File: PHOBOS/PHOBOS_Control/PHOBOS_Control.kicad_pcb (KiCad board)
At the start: 2 copper layers, 125.4 x 71.6 mm, 76 parts, among them J1 Screw_Terminal_01x02, J2 Conn_01x06, J3 Conn_Coaxial, J5 DE9_Pins_MountingHoles, J6 USB4056-03-A_REVA2, U1 SX1280IMLTRT, U2 TLV9351IDCKR, U3 W25Q128JVSIQ, U4 NCP1117-3.3_SOT223, U5 RP2040, U6 TLV9351IDCKR, U7 TLV9351IDCKR, U8 TLV9351IDCKR, Y1 ABM8-272-T3, Y2 C1E-52.000-10-1012-X-M

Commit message: some routing added. op amps rearranged
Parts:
- moved C14 47.2 mm to (138.2, 367.5)
- moved D1 47.2 mm to (143.1, 364.1)
- moved C12 47.2 mm to (139.9, 367.5)
- moved C13 47.2 mm to (141.5, 367.5)
- moved D4 47.2 mm to (143.1, 367.5)
- moved J1 47.2 mm to (146.5, 361.5)
- moved R9 47.2 mm to (133.9, 362.3)
- moved U4 47.2 mm to (138.3, 360.9)
- moved D5 47.2 mm to (132.5, 361.5)
- moved Y2 26.6 mm to (145.2, 397.0)
- moved L1 19.1 mm to (154.2, 391.8)
- moved L2 15.1 mm to (150.4, 390.5)
- moved R15 15.1 mm to (150.4, 392.5)
- moved C37 13.4 mm to (161.9, 364.3)
- moved R12 13.4 mm to (157.4, 364.3)
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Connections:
- C30 pad 1: /PS1MCU -> /PS4MCU
- C31 pad 1: /PS1 -> /PS4
- C32 pad 1: /PS2MCU -> /PS3MCU
- C33 pad 1: /PS2 -> /PS3
- C34 pad 1: /PS3MCU -> /PS2MCU
- C35 pad 1: /PS3 -> /PS2
- C36 pad 1: /PS4MCU -> /PS1MCU
- C37 pad 1: /PS4 -> /PS1
- J5 pad 1: unconnected-(J5-Pad1) -> /PS4
- J5 pad 2: /PS4 -> /PS3
- J5 pad 3: /PS3 -> /PS2
- J5 pad 4: /PS2 -> /PS1
- J5 pad 5: /PS1 -> unconnected-(J5-Pad5)
- R13 pad 2: /PS4 -> /PS1
- R2 pad 2: /PS1 -> /PS4
- R4 pad 2: /PS2 -> /PS3
- R8 pad 2: /PS3 -> /PS2
- U2 pad 1: /PS1MCU -> /PS4MCU
- U2 pad 4: /PS1 -> /PS4
- U5 pad 28: /PS1MCU -> /PS4MCU
- U5 pad 29: /PS2MCU -> /PS3MCU
- U5 pad 30: /PS3MCU -> /PS2MCU
- U5 pad 31: /PS4MCU -> /PS1MCU
- U6 pad 1: /PS2MCU -> /PS3MCU
- U6 pad 4: /PS2 -> /PS3
- U7 pad 1: /PS3MCU -> /PS2MCU
- U7 pad 4: /PS3 -> /PS2
- U8 pad 1: /PS4MCU -> /PS1MCU
- U8 pad 4: /PS4 -> /PS1
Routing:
- net +BATT: track 4.14 -> 39.5 mm, vias 0 -> 4
- net +3V3: track 0.00 -> 22.7 mm
- net /PS1: track 0.00 -> 9.35 mm
- net /PS4: track 0.00 -> 7.32 mm
- net /PS2: track 0.00 -> 7.28 mm
- net /PS3: track 0.00 -> 6.65 mm
- net +1V1: track 0.00 -> 6.18 mm
- net Net-(U6--): track 0.00 -> 2.54 mm
- net Net-(U2--): track 0.00 -> 2.52 mm
- net Net-(U8--): track 0.00 -> 2.42 mm
- net Net-(U7--): track 0.00 -> 2.40 mm
- net /PS4MCU: track 0.00 -> 1.52 mm
- net /PS3MCU: track 0.00 -> 1.43 mm
- net /PS2MCU: track 0.00 -> 1.39 mm
- net /PS1MCU: track 0.00 -> 1.25 mm
- added copper zone on B.Cu, net GND

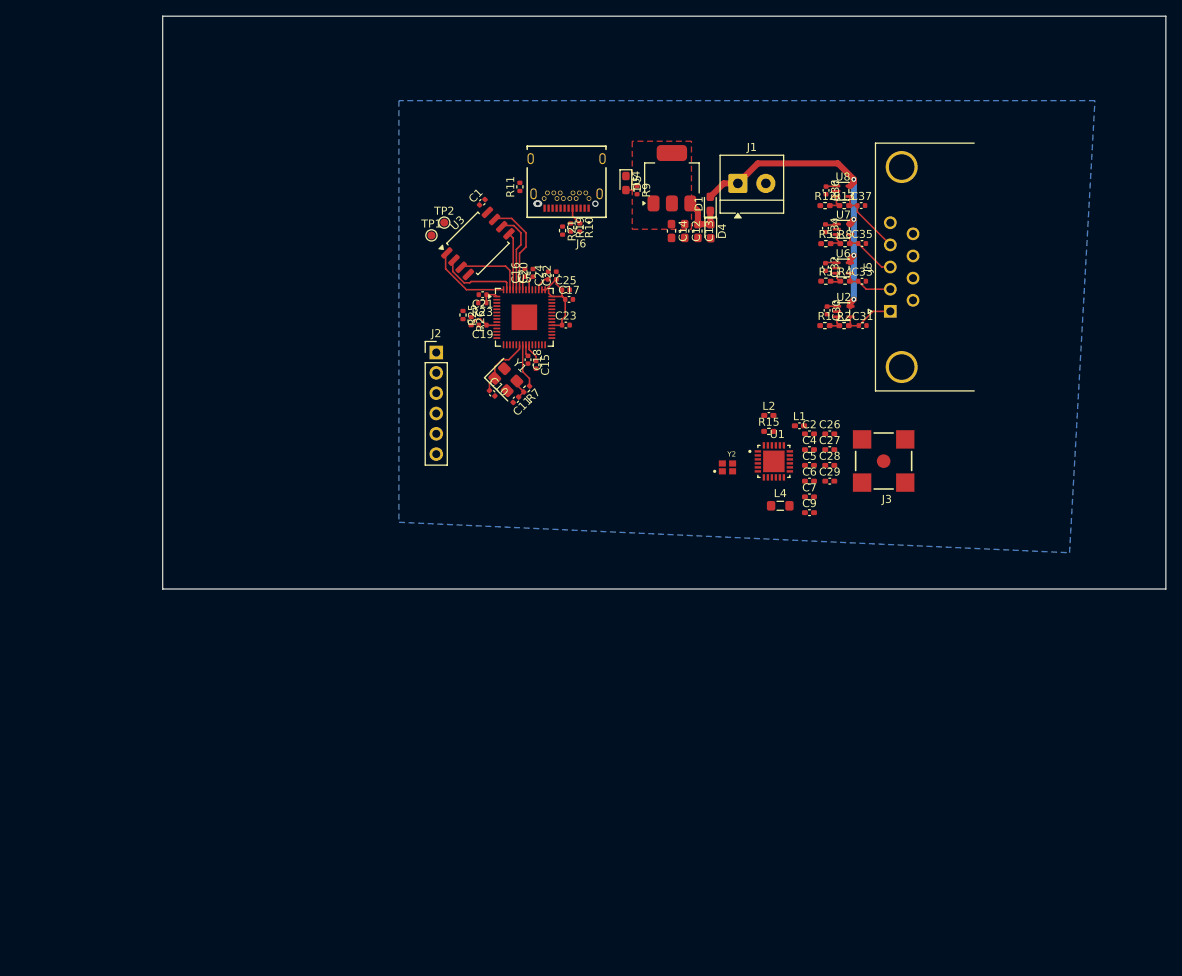
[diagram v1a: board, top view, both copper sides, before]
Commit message: USB Routed, routing updated
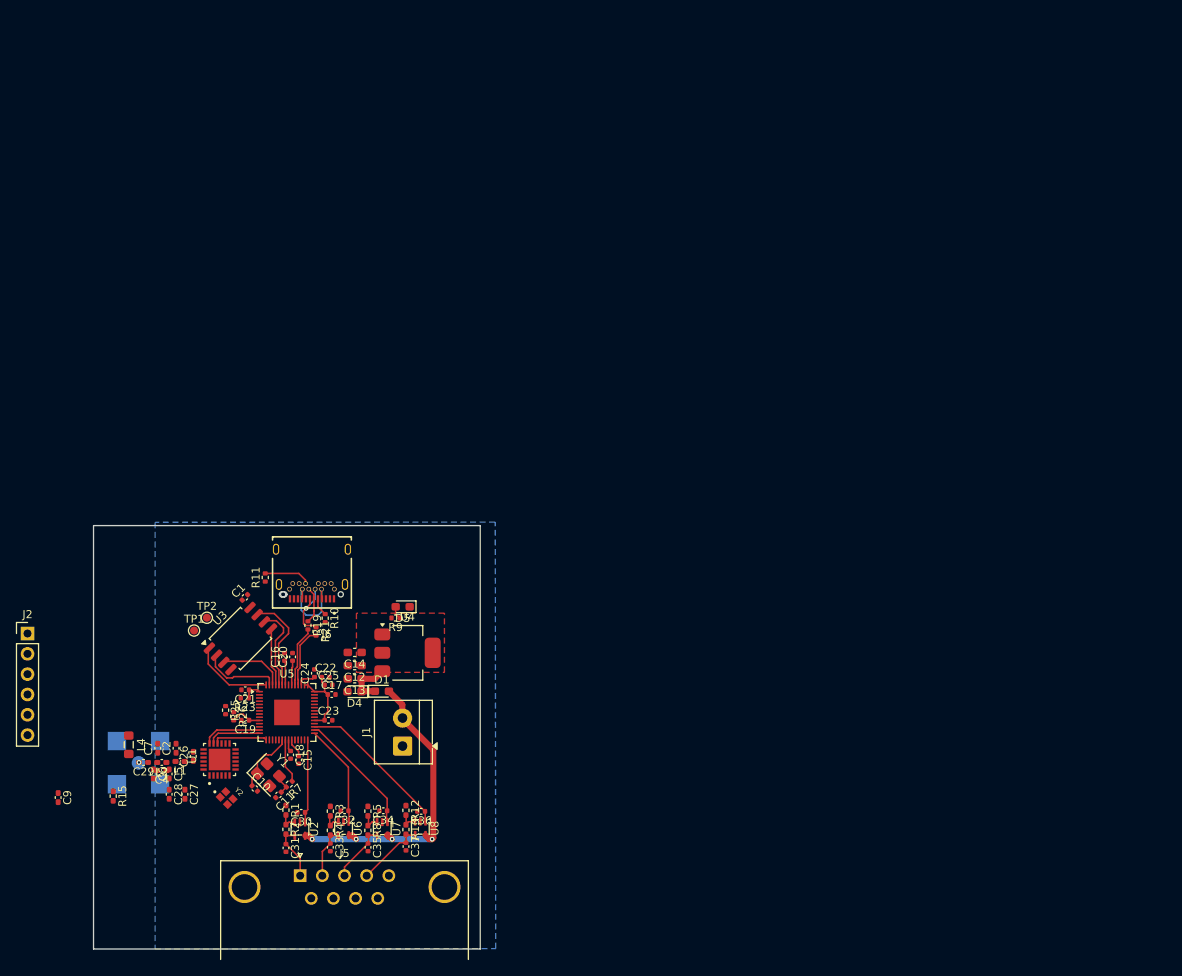
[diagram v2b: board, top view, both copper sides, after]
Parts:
- J3: moved to B.Cu
- moved J5 102.1 mm to (91.8, 448.0), turned to 0 degrees
- moved J3 100.5 mm to (71.6, 433.9), turned to 0 degrees
- moved C9 100.4 mm to (61.5, 438.3), turned to -90 degrees
- moved C37 98.3 mm to (105.0, 444.4), turned to -90 degrees
- moved C35 97.5 mm to (100.3, 444.5), turned to -90 degrees
- moved C31 97.3 mm to (90.0, 444.6), turned to -90 degrees
- moved C33 97.1 mm to (95.6, 444.5), turned to -90 degrees
- moved U8 95.6 mm to (106.8, 442.1), turned to -90 degrees
- moved R13 95.3 mm to (105.0, 442.3), turned to -90 degrees
- moved U7 94.5 mm to (102.1, 442.2), turned to -90 degrees
- moved R8 94.5 mm to (100.3, 442.4), turned to -90 degrees
- moved R4 94.1 mm to (95.6, 442.4), turned to -90 degrees
- moved R2 94.0 mm to (90.0, 442.2), turned to -90 degrees
- moved U6 93.9 mm to (97.2, 442.1), turned to -90 degrees
- moved U2 93.8 mm to (91.8, 442.2), turned to -90 degrees
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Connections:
- J1 pad 1: +BATT -> GND
- J1 pad 2: GND -> +BATT
- J5 pad 1: /PS4 -> unconnected-(J5-Pad1)
- J5 pad 2: /PS3 -> /PS1
- J5 pad 4: /PS1 -> /PS3
- J5 pad 5: unconnected-(J5-Pad5) -> /PS4
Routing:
- net /PS1MCU: track 1.25 -> 19.4 mm
- net /PS2MCU: track 1.39 -> 15.6 mm
- net /PS3MCU: track 1.43 -> 12.9 mm
- net VBUS: track 0.00 -> 11.0 mm
- net /PS4MCU: track 1.52 -> 10.7 mm
- net /USB_D-: track 0.00 -> 8.05 mm, vias 0 -> 1
- net /USB_+: track 0.00 -> 7.61 mm
- net /USB_-: track 0.00 -> 7.59 mm
- net /SCK: track 0.00 -> 7.39 mm
- net /MISO: track 0.00 -> 6.85 mm
- net /MOSI: track 0.00 -> 6.69 mm
- net Net-(J6-CC2): track 0.00 -> 5.81 mm
- net /USB_D+: track 0.00 -> 4.60 mm
- net +1V1: track 6.18 -> 7.80 mm
- net +3V3: track 22.7 -> 21.4 mm
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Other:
- board size 125.4 x 71.6 mm -> 48.3 x 52.9 mm

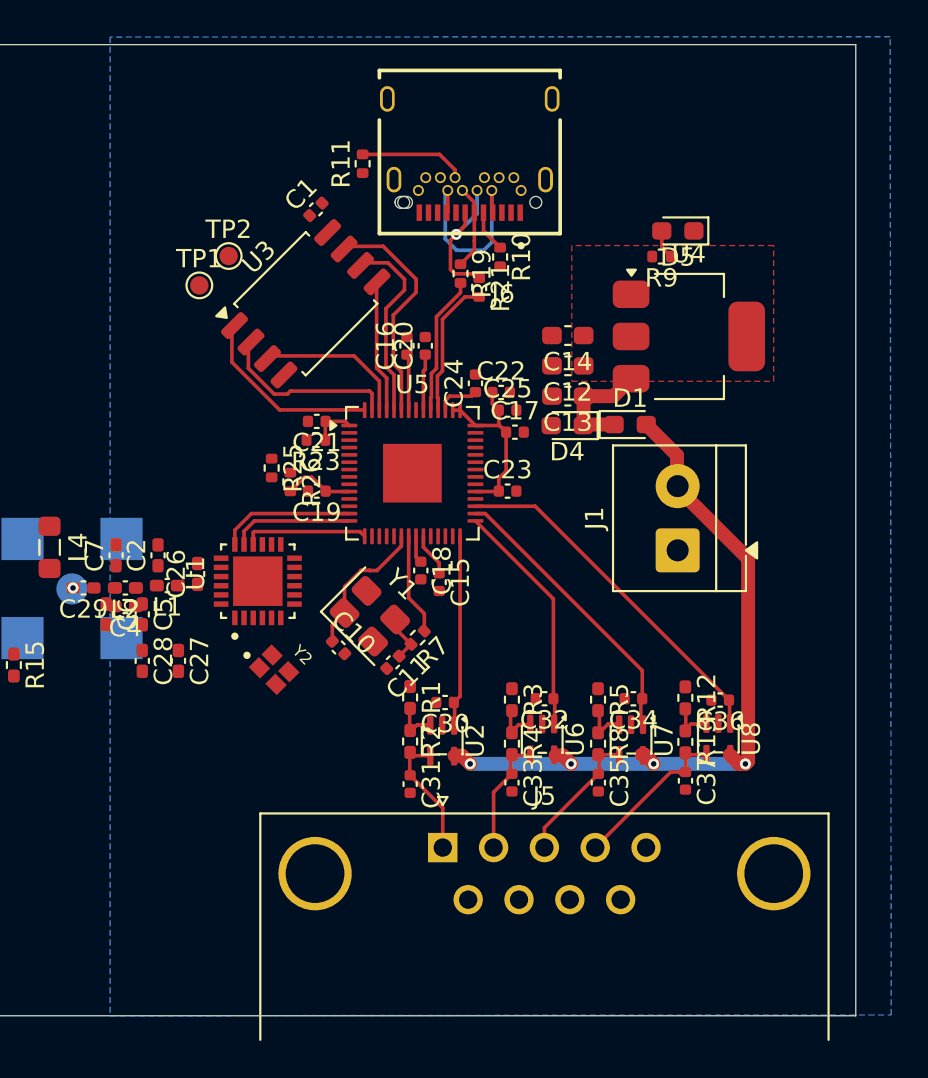
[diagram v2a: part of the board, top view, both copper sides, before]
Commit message: repalced with 4-pin connector
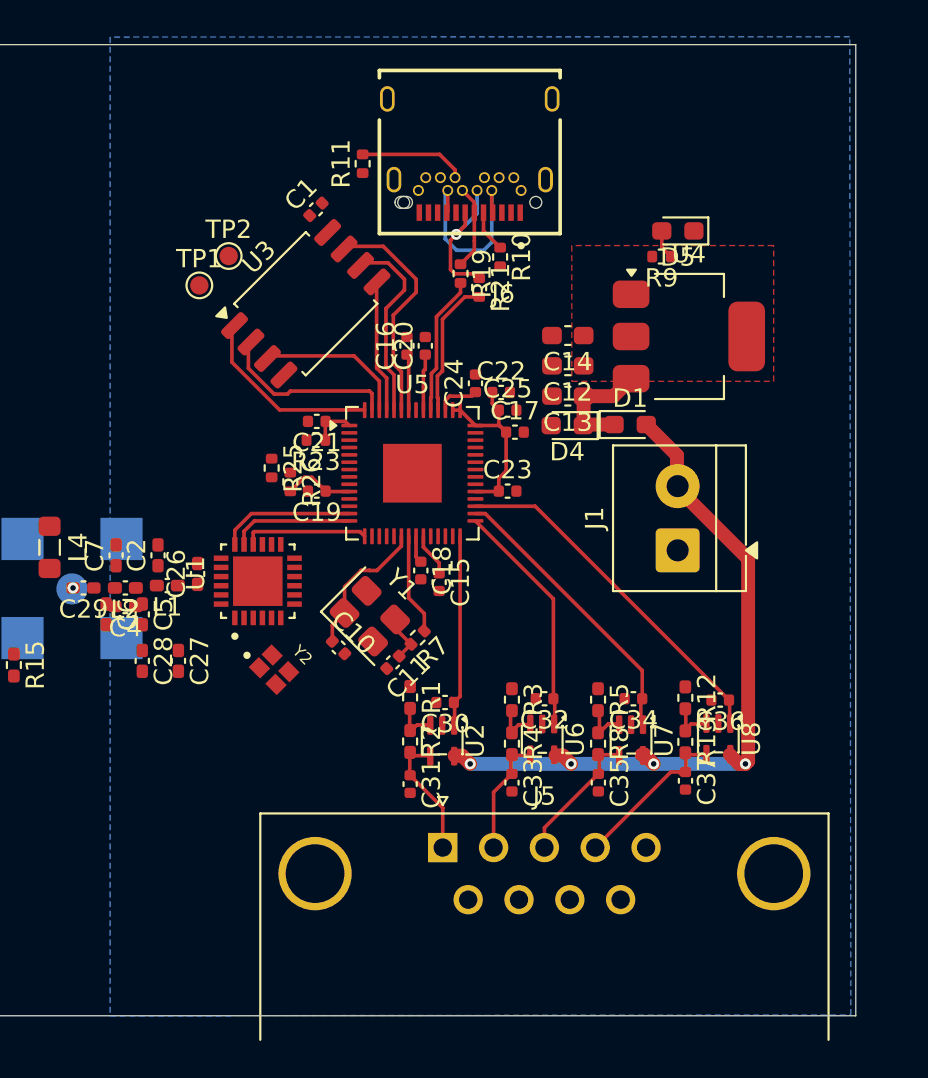
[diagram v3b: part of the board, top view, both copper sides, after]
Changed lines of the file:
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@@
 		)
 		(min_thickness 0.25)
-		(fill yes
+		(fill
 			(thermal_gap 0.5)
 			(thermal_bridge_width 0.5)
@@
 		(polygon
 			(pts
-				(xy 116.173781 403.83889) (xy 73.66 403.86) (xy 73.66 457.2) (xy 116.232717 457.152938)
+				(xy 113.970529 403.839984) (xy 73.66 403.86) (xy 73.66 457.2) (xy 114.029466 457.155374)
 			)
 		)

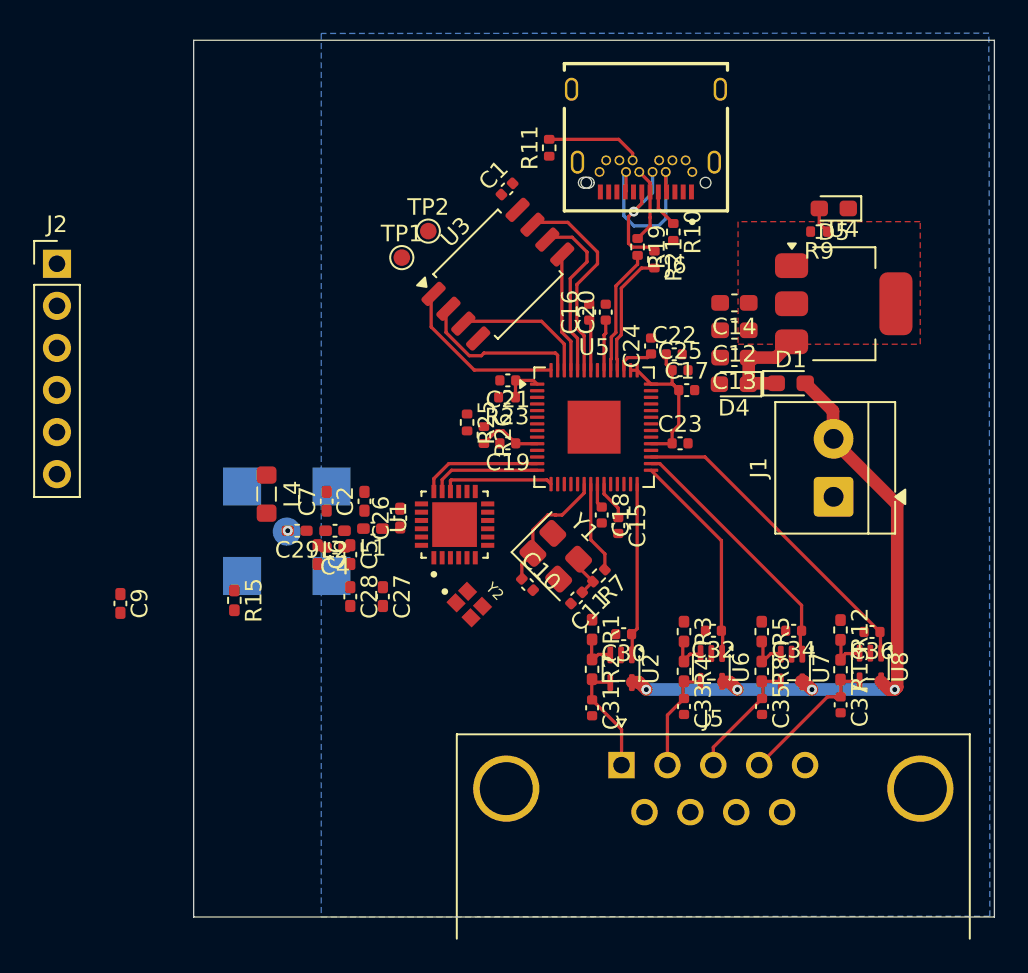
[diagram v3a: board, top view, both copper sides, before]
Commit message: design blocks tested. connectors added
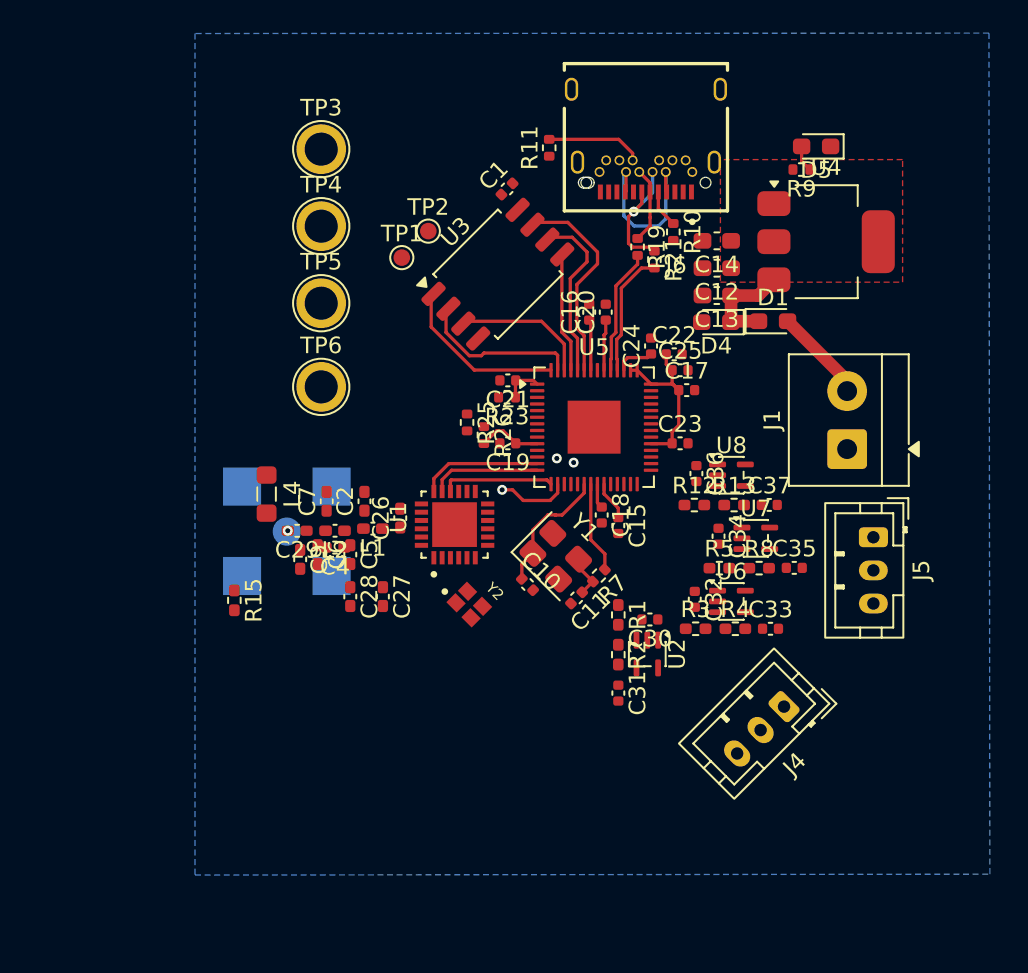
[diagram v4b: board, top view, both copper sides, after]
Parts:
- removed J2: Conn_01x06, Connector_PinHeader_2.54mm:PinHeader_1x06_P2.54mm_Vertical
- added J4: Conn_01x03, Connector_JST:JST_PH_B3B-PH-K_1x03_P2.00mm_Vertical, F.Cu at (101.6, 444.5)
- added TP3: SCK, TestPoint:TestPoint_Plated_Hole_D2.0mm, F.Cu at (73.7, 410.8)
- added TP4: MOSI, TestPoint:TestPoint_Plated_Hole_D2.0mm, F.Cu at (73.7, 415.5)
- added TP5: MISO, TestPoint:TestPoint_Plated_Hole_D2.0mm, F.Cu at (73.7, 420.1)
- added TP6: CS, TestPoint:TestPoint_Plated_Hole_D2.0mm, F.Cu at (73.7, 425.2)
- J5: value DE9_Pins_MountingHoles -> Conn_01x03; footprint Connector_Dsub:DSUB-9_Pins_Horizontal_P2.77x2.84mm_EdgePinOffset7.70mm_Housed_MountingHolesOffset9.12mm -> Connector_JST:JST_PH_B3B-PH-K_1x03_P2.00mm_Vertical
- moved J5 20.5 mm to (107.0, 434.3), turned to -90 degrees
- moved U8 14.3 mm to (98.4, 430.5), turned to 0 degrees
- moved C36 14.3 mm to (96.3, 430.4), turned to -90 degrees
- moved C37 12.8 mm to (100.7, 432.3), turned to 0 degrees
- moved R13 11.8 mm to (98.6, 432.3), turned to 0 degrees
- moved R12 11.6 mm to (96.2, 432.3), turned to 0 degrees
- moved C9 11.2 mm to (72.4, 435.6)
- moved C35 8.59 mm to (102.2, 436.1), turned to 0 degrees
- moved U7 8.12 mm to (99.9, 434.3), turned to 0 degrees
- moved C34 7.29 mm to (97.6, 434.2), turned to -90 degrees
- moved C33 7.02 mm to (100.8, 439.8), turned to 0 degrees
- moved R8 6.23 mm to (100.1, 436.1), turned to 0 degrees
- moved R5 4.61 mm to (97.7, 436.1), turned to 0 degrees
- moved U6 4.16 mm to (98.4, 438.1), turned to 0 degrees
- moved R4 4.03 mm to (98.7, 439.8), turned to 0 degrees
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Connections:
- C27 pad 1: VDD -> +3V3
- J5 pad 1: unconnected-(J5-Pad1) -> /PS1
- J5 pad 2: /PS1 -> /PS2
- J5 pad 3: /PS2 -> GND
- R15 pad 2: VDD -> +3V3
- U1 pad 15: VDD -> +3V3
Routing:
- net +BATT: track 39.9 -> 5.71 mm, vias 4 -> 0
- net /PS1MCU: track 19.4 -> 0.00 mm
- net /PS2MCU: track 15.6 -> 0.00 mm
- net /PS3MCU: track 12.9 -> 0.00 mm
- net /PS4MCU: track 10.7 -> 0.00 mm
- net /PS1: track 9.35 -> 0.00 mm
- net /PS4: track 7.32 -> 0.00 mm
- net /PS2: track 7.28 -> 0.00 mm
- net /PS3: track 6.65 -> 0.00 mm
- net /NSS: track 0.00 -> 4.34 mm, vias 0 -> 1
- net Net-(U6--): track 2.54 -> 0.00 mm
- net Net-(U2--): track 2.52 -> 0.00 mm
- net Net-(U8--): track 2.42 -> 0.00 mm
- net Net-(U7--): track 2.40 -> 0.00 mm
- net (no net): vias 0 -> 2
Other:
- board size 48.3 x 52.9 mm -> 1 x 0.6 mm
